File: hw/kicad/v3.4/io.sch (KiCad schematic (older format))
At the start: 4 parts

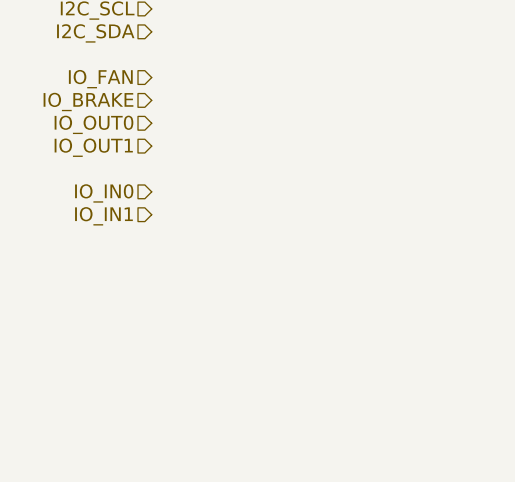
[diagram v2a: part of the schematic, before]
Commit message: io +spi
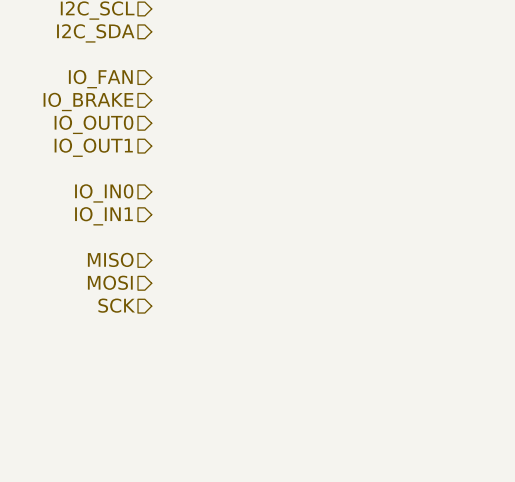
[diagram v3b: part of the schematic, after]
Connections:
- net labels added: MISO, MOSI, SCK
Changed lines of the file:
@@
 $Descr A4 11693 8268
 encoding utf-8
-Sheet 11 15
+Sheet 15 15
 Title ""
 Date ""
@@
 	1    0    0    -1
 $EndComp
+Text HLabel 4400 4200 0    60   Input ~ 0
+MISO
+Text HLabel 4400 4300 0    60   Input ~ 0
+MOSI
+Text HLabel 4400 4400 0    60   Input ~ 0
+SCK
 $EndSCHEMATC

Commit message: expand io header
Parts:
- removed P?: CONN_02X05, symbol CONN_02X05
- added P?: CONN_02X10, symbol CONN_02X10
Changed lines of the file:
@@
 EESchema Schematic File Version 2
-LIBS:power
+LIBS:conn
 LIBS:stmbl_3.4-cache
 EELAYER 25 0
@@
 Text HLabel 4400 4000 0    60   Input ~ 0
 IO_IN1
-$Comp
-L CONN_02X05 P?
-U 1 1 566847FE
-P 8000 4500
-F 0 "P?" H 8000 4800 50  0000 C CNN
-F 1 "CONN_02X05" H 8000 4200 50  0000 C CNN
-F 2 "" H 8000 3300 60  0000 C CNN
-F 3 "" H 8000 3300 60  0000 C CNN
-	1    8000 4500
-	1    0    0    -1
-$EndComp
 Text HLabel 4400 4200 0    60   Input ~ 0
 MISO
@@
 Text HLabel 4400 4400 0    60   Input ~ 0
 SCK
+$Comp
+L CONN_02X10 P?
+U 1 1 566AF491
+P 8000 4700
+F 0 "P?" H 8000 5250 50  0000 C CNN
+F 1 "CONN_02X10" V 8000 4700 50  0000 C CNN
+F 2 "" H 8000 3500 50  0000 C CNN
+F 3 "" H 8000 3500 50  0000 C CNN
+	1    8000 4700
+	1    0    0    -1
+$EndComp
 $EndSCHEMATC

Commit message: hw v3.4
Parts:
- added C? (x3): C, symbol C
- added U? (x3): USBLC6-4SC6, symbol USBLC6-4SC6
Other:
- moved on the sheet: P?
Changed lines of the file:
@@
 EESchema Schematic File Version 2
 LIBS:conn
+LIBS:power
 LIBS:stmbl_3.4-cache
 EELAYER 25 0
@@
 	1    0    0    -1
 $EndComp
-Text HLabel 4400 2400 0    60   Input ~ 0
+Text HLabel 5700 1600 0    60   Input ~ 0
 CAN_TX
-Text HLabel 4400 2500 0    60   Input ~ 0
+Text HLabel 5700 1700 0    60   Input ~ 0
 CAN_RX
-Text HLabel 4400 2700 0    60   Input ~ 0
+Text HLabel 5700 1800 0    60   Input ~ 0
 TX
-Text HLabel 4400 2800 0    60   Input ~ 0
+Text HLabel 5700 1900 0    60   Input ~ 0
 RX
-Text HLabel 4400 2900 0    60   Input ~ 0
+Text HLabel 5700 2000 0    60   Input ~ 0
 CK
-Text HLabel 4400 3100 0    60   Input ~ 0
+Text HLabel 5700 2100 0    60   Input ~ 0
 I2C_SCL
-Text HLabel 4400 3200 0    60   Input ~ 0
+Text HLabel 5700 2200 0    60   Input ~ 0
 I2C_SDA
 Text HLabel 4400 3400 0    60   Input ~ 0
@@
 Text HLabel 4400 4000 0    60   Input ~ 0
 IO_IN1
-Text HLabel 4400 4200 0    60   Input ~ 0
+Text HLabel 5700 2300 0    60   Input ~ 0
 MISO
-Text HLabel 4400 4300 0    60   Input ~ 0
+Text HLabel 5700 2400 0    60   Input ~ 0
 MOSI
-Text HLabel 4400 4400 0    60   Input ~ 0
+Text HLabel 5700 2500 0    60   Input ~ 0
 SCK
 $Comp
 L CONN_02X10 P?
 U 1 1 566AF491
-P 8000 4700
-F 0 "P?" H 8000 5250 50  0000 C CNN
-F 1 "CONN_02X10" V 8000 4700 50  0000 C CNN
-F 2 "" H 8000 3500 50  0000 C CNN
-F 3 "" H 8000 3500 50  0000 C CNN
-	1    8000 4700
+P 6650 2050
+F 0 "P?" H 6650 2600 50  0000 C CNN
+F 1 "CONN_02X10" V 6650 2050 50  0000 C CNN
+F 2 "" H 6650 850 50  0000 C CNN
+F 3 "" H 6650 850 50  0000 C CNN
+	1    6650 2050
 	1    0    0    -1
 $EndComp
+Text HLabel 4400 4100 0    60   Input ~ 0
+IO_IN2
+Text HLabel 4400 4200 0    60   Input ~ 0
+IO_IN3
+$Comp
+L USBLC6-4SC6 U?
+U 1 1 56819D62
+P 4650 5100
+F 0 "U?" H 3951 5448 50  0000 C CNN
+F 1 "USBLC6-4SC6" H 4650 5350 50  0000 C CNN
+F 2 "" H 4650 5100 60  0000 C CNN
+F 3 "" H 4650 5100 60  0000 C CNN
+F 4 "TRANSIENT VOLTAGE SUPPRESSOR" H 4650 4850 50  0000 C CNN "Description"
+	1    4650 5100
+	1    0    0    -1
+$EndComp
+$Comp
+L USBLC6-4SC6 U?
+U 1 1 56819DA2
+P 4650 5800
+F 0 "U?" H 3951 6148 50  0000 C CNN
+F 1 "USBLC6-4SC6" H 4650 6050 50  0000 C CNN
+F 2 "" H 4650 5800 60  0000 C CNN
+F 3 "" H 4650 5800 60  0000 C CNN
+F 4 "TRANSIENT VOLTAGE SUPPRESSOR" H 4650 5550 50  0000 C CNN "Description"
+	1    4650 5800
+	1    0    0    -1
+$EndComp
+$Comp
+L USBLC6-4SC6 U?
+U 1 1 56819DFD
+P 4650 6500
+F 0 "U?" H 3951 6848 50  0000 C CNN
+F 1 "USBLC6-4SC6" H 4650 6750 50  0000 C CNN
+F 2 "" H 4650 6500 60  0000 C CNN
+F 3 "" H 4650 6500 60  0000 C CNN
+F 4 "TRANSIENT VOLTAGE SUPPRESSOR" H 4650 6250 50  0000 C CNN "Description"
+	1    4650 6500
+	1    0    0    -1
+$EndComp
+$Comp
+L C C?
+U 1 1 56819E35
+P 3300 5050
+F 0 "C?" H 3325 5150 50  0000 L CNN
+F 1 "C" H 3325 4950 50  0000 L CNN
+F 2 "" H 3338 4900 30  0000 C CNN
+F 3 "" H 3300 5050 60  0000 C CNN
+	1    3300 5050
+	1    0    0    -1
+$EndComp
+$Comp
+L C C?
+U 1 1 56819EA9
+P 3300 5750
+F 0 "C?" H 3325 5850 50  0000 L CNN
+F 1 "C" H 3325 5650 50  0000 L CNN
+F 2 "" H 3338 5600 30  0000 C CNN
+F 3 "" H 3300 5750 60  0000 C CNN
+	1    3300 5750
+	1    0    0    -1
+$EndComp
+$Comp
+L C C?
+U 1 1 56819EF3
+P 3300 6450
+F 0 "C?" H 3325 6550 50  0000 L CNN
+F 1 "C" H 3325 6350 50  0000 L CNN
+F 2 "" H 3338 6300 30  0000 C CNN
+F 3 "" H 3300 6450 60  0000 C CNN
+	1    3300 6450
+	1    0    0    -1
+$EndComp

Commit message: hw v3.4
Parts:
- added D? (x4): D, symbol D
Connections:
- net IO_BRAKE: now also P?.2 (P2), D?.2 (A)
- net IO_FAN: now also P?.2 (P2), D?.2 (A)
- net IO_IN0: now also P?.2 (P2)
- net IO_IN1: now also P?.5 (P5)
- net IO_OUT0: now also P?.4 (P4), D?.2 (A)
- net IO_OUT1: now also P?.6 (P6), D?.2 (A)
- net +24V: now reaches P?.1 (P1)
- net +24V: now also P?.1 (P1), P?.1 (P1), P?.3 (P3), P?.4 (P4), P?.5 (P5), D?.1 (K), D?.1 (K), D?.1 (K), D?.1 (K)
- net GND: now reaches P?.3 (P3)
- net GND: now also P?.6 (P6)
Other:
- moved on the sheet: P?

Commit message: v3.4
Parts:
- removed D? (x4): D, symbol D
- added D? (x4): D, symbol D
- added JP?: JUMPER3, symbol JUMPER3
- added Q? (x4): IRLML6344, SOT-23, symbol MMBF170
- added R? (x4): 22, symbol R
- added R? (x4): 1k, symbol R
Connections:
- net +12V: now also JP?.1
- net +24V: now also D?.1 (K), D?.1 (K), D?.1 (K), JP?.3; no longer P?.1 (P1)
- net GND: now also Q?.2 (S), Q?.2 (S), Q?.2 (S), Q?.2 (S), R?.2, R?.2, R?.2, R?.2
- net IO_BRAKE: now also R?.2; no longer P?.2 (P2)
- net IO_FAN: now also R?.2; no longer P?.2 (P2)
- net IO_OUT0: now also R?.2; no longer P?.4 (P4)
- net IO_OUT1: now also R?.2; no longer P?.6 (P6)
- new net: D?.1 (K), JP?.2, P?.1 (P1)
- new net: D?.2 (A), P?.2 (P2), Q?.3 (D) (x2)
- new net: D?.2 (A), P?.4 (P4), Q?.3 (D)
- new net: D?.2 (A), P?.6 (P6), Q?.3 (D)
- new net: Q?.1 (G), R?.1, R?.1 (x4)
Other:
- moved on the sheet: C?, P?, U?
